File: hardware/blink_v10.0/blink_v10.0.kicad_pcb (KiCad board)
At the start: 2 copper layers, 119 x 92 mm, 130 parts, among them J1 Conn_01x02, J11 KH-BNC50-3511, J12 KH-BNC50-3511, J13 KH-BNC50-3511, J14 Conn_02x16_Odd_Even, J15 Conn_01x01, J16 Conn_01x01, J2 PJ-320D, J3 PJ-320D, J4 KH-BNC50-3511, J5 Conn_01x06_Pin, J6 Conn_01x03, J7 Conn_01x06_Pin, J9 USB_C_Receptacle, Q1 S8550, Q2 S8050, Q3 2N7002, Q4 2N7002, Q5 2N7002, SW1 SW_SPDT, SW3 LC1258OASP, SW4 SW_Push_4PDT, SW5 LC1258OASP, U1 AMS1117-3.3, U10 TMP102xxDRL, U2 AD8397, U3 M24C02-RMN, U4 STM32F405RGTx, U5 SN74LVC1G14DBV, U6 SN74LVC1G14DBV, U7 CH340C, U8 USBLC6-2P6, U9 MCP73832-2-OT, X1 GTXO-14V (2.048MHz), Y1 16MHz

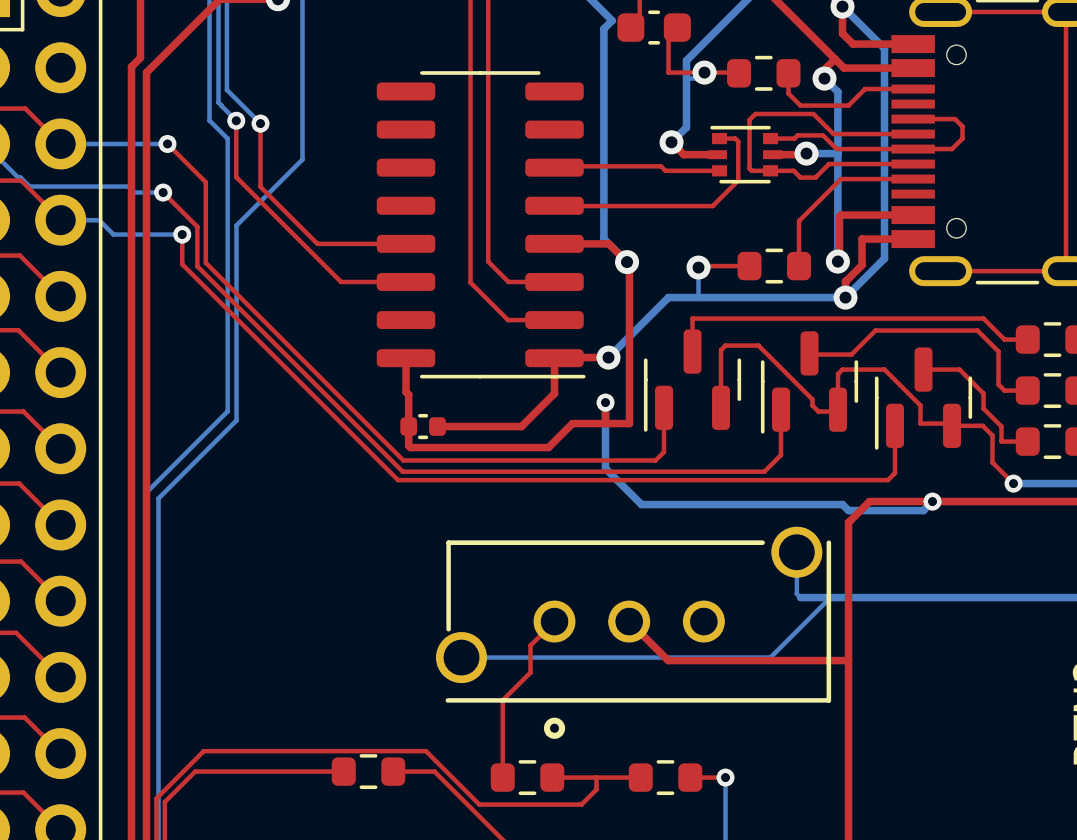
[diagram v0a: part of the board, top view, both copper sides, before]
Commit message: Fixes #211 led setting when not running
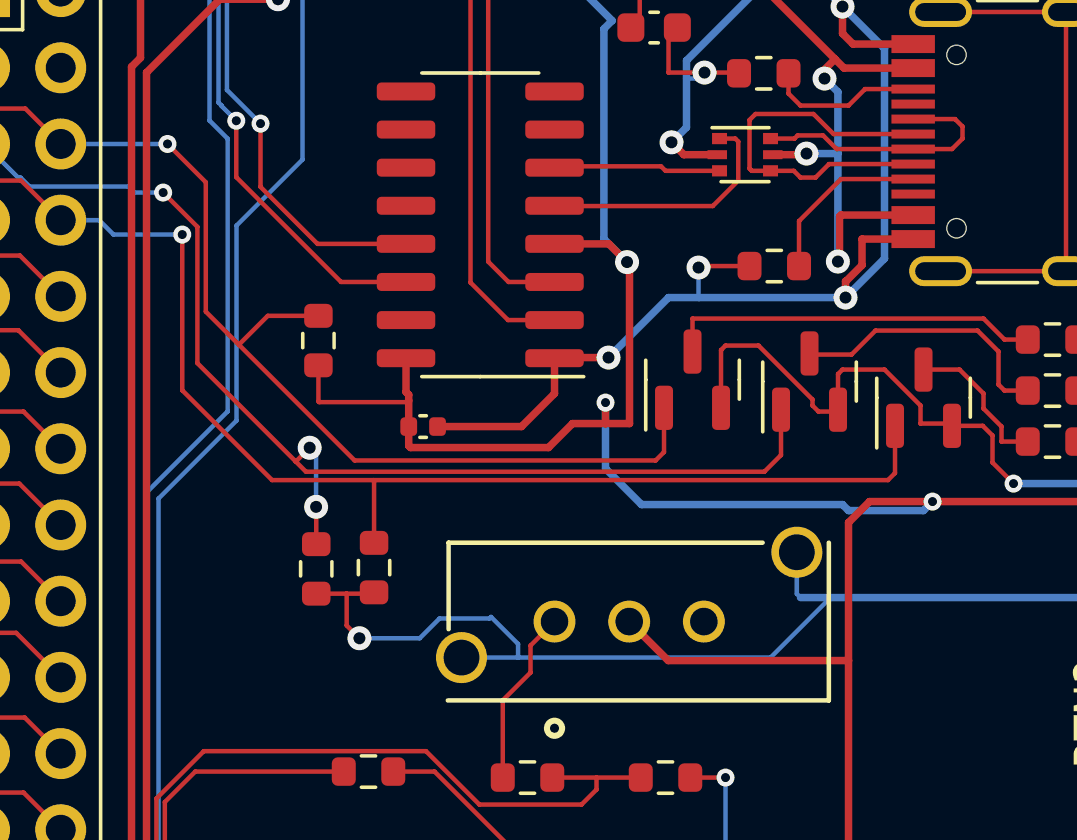
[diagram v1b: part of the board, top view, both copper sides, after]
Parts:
- added R51: 47K, Resistor_SMD:R_0603_1608Metric, F.Cu at (202.1, 72.6)
- added R52: 47K, Resistor_SMD:R_0603_1608Metric, F.Cu at (202.1, 80.2)
- added R53: 47K, Resistor_SMD:R_0603_1608Metric, F.Cu at (204.0, 80.2)
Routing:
- net GND: track 1119.8 -> 1129.8 mm, vias 46 -> 47
- net /LEDMG: track 73.8 -> 79.6 mm, vias 1 -> 3
- net /LEDMY: track 87.0 -> 91.5 mm
- net +3.3V: track 528.6 -> 532.9 mm
- net /LEDMR: track 71.7 -> 75.7 mm

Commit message: change LEDMY to LEDMB. Fixes #230
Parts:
- R21, R22: value 5k1 -> 5K1
- U10: value TMP102xxDRL -> TMP112AIDRLR
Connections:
- net /LEDMY renamed /LEDMB
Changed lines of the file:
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@@
   (net 14 "/Mic")
   (net 15 "/BOOT1")
-  (net 16 "/LEDMY")
+  (net 16 "/LEDMB")
   (net 17 "/NCOL3")
   (net 18 "/NCOL2")
@@
       (stroke (width 0.1) (type solid)) (layer "F.Fab"))
     (pad "1" smd roundrect (at -0.9375 -0.95 90) (size 1.475 0.6) (layers "F.Cu" "F.Paste" "F.Mask") (roundrect_rratio 0.25)
-      (net 16 "/LEDMY") (pinfunction "G") (pintype "input"))
+      (net 16 "/LEDMB") (pinfunction "G") (pintype "input"))
     (pad "2" smd roundrect (at -0.9375 0.95 90) (size 1.475 0.6) (layers "F.Cu" "F.Paste" "F.Mask") (roundrect_rratio 0.25)
       (net 21 "GND") (pinfunction "S") (pintype "passive"))
@@
       (net 11 "/NCOL1") (pinfunction "Pin_7") (pintype "passive"))
     (pad "8" thru_hole oval locked (at 2.54 7.62) (size 1.7 1.7) (drill 1) (layers "*.Cu" "*.Mask")
-      (net 16 "/LEDMY") (pinfunction "Pin_8") (pintype "passive"))
+      (net 16 "/LEDMB") (pinfunction "Pin_8") (pintype "passive"))
     (pad "9" thru_hole oval locked (at 0 10.16) (size 1.7 1.7) (drill 1) (layers "*.Cu" "*.Mask")
       (net 17 "/NCOL3") (pinfunction "Pin_9") (pintype "passive"))
@@
     (descr "SOT563")
     (tags "SOT-563")
-    (property "JLCPCB Part #" "C99269")
+    (property "JLCPCB Part #" "C28927")
+    (property "JLCPCB Rotation Offset" "180")
     (property "Sheetfile" "blink_v10.0.kicad_sch")
     (property "Sheetname" "")
@@
         (effects (font (size 1 1) (thickness 0.15)))
     )
-    (fp_text value "TMP102xxDRL" (at 0 1.75) (layer "F.Fab")
+    (fp_text value "TMP112AIDRLR" (at 0 1.75) (layer "F.Fab")
         (effects (font (size 1 1) (thickness 0.15)))
     )
@@
         (effects (font (size 1 1) (thickness 0.15)))
     )
-    (fp_text value "5k1" (at 0 1.43) (layer "F.Fab")
+    (fp_text value "5K1" (at 0 1.43) (layer "F.Fab")
         (effects (font (size 1 1) (thickness 0.15)))
     )
@@
         (effects (font (size 1 1) (thickness 0.15)))
     )
-    (fp_text value "5k1" (at 0 1.43) (layer "F.Fab")
+    (fp_text value "5K1" (at 0 1.43) (layer "F.Fab")
         (effects (font (size 1 1) (thickness 0.15)))
     )
@@
       (net 11 "/NCOL1") (pinfunction "PB6") (pintype "bidirectional"))
     (pad "59" smd roundrect (at -1.25 -5.675 90) (size 0.3 1.55) (layers "F.Cu" "F.Paste" "F.Mask") (roundrect_rratio 0.25)
-      (net 16 "/LEDMY") (pinfunction "PB7") (pintype "bidirectional"))
+      (net 16 "/LEDMB") (pinfunction "PB7") (pintype "bidirectional"))
     (pad "60" smd roundrect (at -1.75 -5.675 90) (size 0.3 1.55) (layers "F.Cu" "F.Paste" "F.Mask") (roundrect_rratio 0.25)
       (net 45 "/BOOT0") (pinfunction "BOOT0") (pintype "input"))
@@
       (net 21 "GND") (pintype "passive"))
     (pad "2" smd roundrect (at 0.825 0 90) (size 0.8 0.95) (layers "F.Cu" "F.Paste" "F.Mask") (roundrect_rratio 0.25)
-      (net 16 "/LEDMY") (pintype "passive"))
+      (net 16 "/LEDMB") (pintype "passive"))
     (model "${KICAD6_3DMODEL_DIR}/Resistor_SMD.3dshapes/R_0603_1608Metric.wrl"
       (offset (xyz 0 0 0))

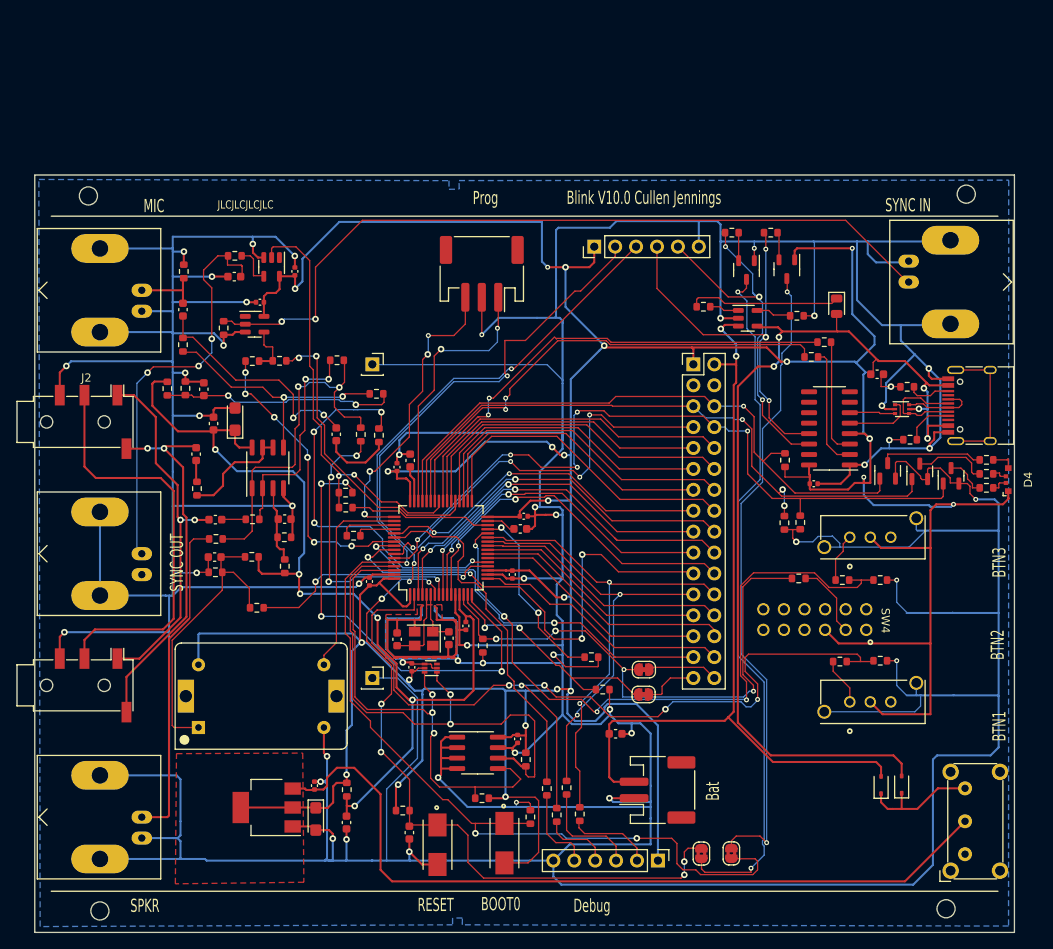
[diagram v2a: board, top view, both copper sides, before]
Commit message: clean up LED5/6 problem and BTN2
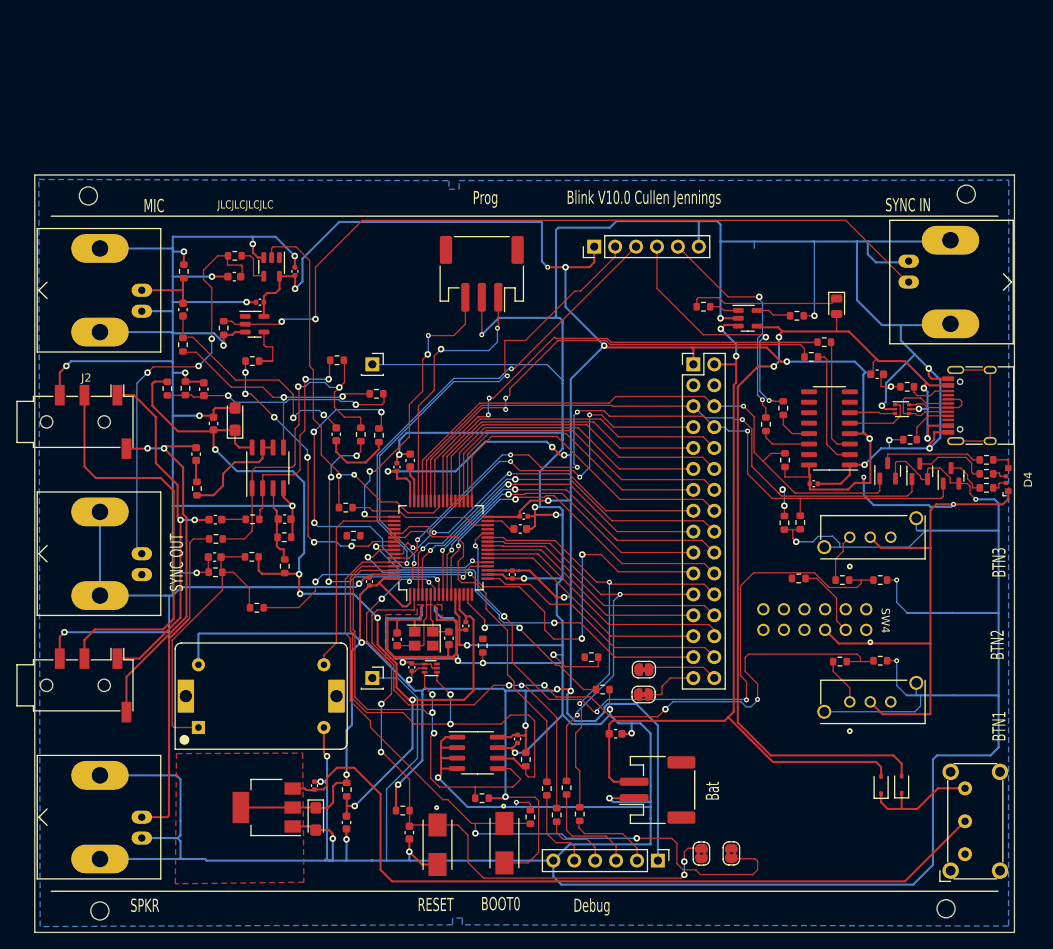
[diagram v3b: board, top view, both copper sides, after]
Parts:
- removed Q1: S8550, Package_TO_SOT_SMD:SOT-23-3
- removed Q2: S8050, Package_TO_SOT_SMD:SOT-23-3
- removed R37, R38: 1K0, Resistor_SMD:R_0603_1608Metric
- moved R29 59.6 mm to (199.8, 68.3), turned to -90 degrees
- moved R20 54.1 mm to (201.9, 66.3), turned to 90 degrees
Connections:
- JP1 pad 1: /AUX_GPS_PPS -> /GPS_TX1
- JP2 pad 1: /AUX_CLK -> /GPS_RX1
- JP3 pad 2: Net-(JP3-B) -> unconnected-(JP3-B-Pad2)
- JP4 pad 2: Net-(JP4-B) -> unconnected-(JP4-B-Pad2)
- R20 pad 1: PPS_OUT -> Net-(U7-~{DTR})
- R20 pad 2: /AUX_MON_PPS -> /USB_DTR
- R26 pad 1: /GPS_TX1 -> /AUX_MON_PPS
- R26 pad 2: /GPS_RX1 -> GND
- R29 pad 1: AUX_SYNC_IN -> /USB_RTS
- R29 pad 2: Net-(R28-Pad2) -> Net-(U7-~{RTS})
- R31 pad 1: /GPS_PPS -> /AUX_CLK
- R33 pad 1: /AUX_CLK -> /AUX_SYNC_IN
- R35 pad 2: /AUX_CLK -> /GPS_PPS
- U4 pad 37: AUX_SYNC_IN -> /AUX_SYNC_IN
- U7 pad 13: /USB_DTR -> Net-(U7-~{DTR})
- U7 pad 14: /USB_RTS -> Net-(U7-~{RTS})
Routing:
- net Net-(JP3-B): track 84.6 -> 0.00 mm, vias 2 -> 0
- net Net-(JP4-B): track 78.2 -> 0.00 mm, vias 2 -> 0
- net /AUX_CLK: track 66.8 -> 0.00 mm, vias 4 -> 0
- net /AUX_MON_PPS: track 56.3 -> 0.00 mm, vias 4 -> 0
- net AUX_SYNC_IN: track 36.4 -> 0.00 mm, vias 2 -> 0
- net +3.3V: track 532.9 -> 508.7 mm, vias 22 -> 21
- net /GPS_PPS: track 22.9 -> 0.00 mm, vias 2 -> 0
- net /USB_DTR: track 49.6 -> 31.1 mm, vias 3 -> 2
- net /USB_RTS: track 45.0 -> 28.3 mm, vias 3 -> 2
- net /AUX_GPS_PPS: track 30.7 -> 21.8 mm
- net /GPS_RX1: track 6.84 -> 0.00 mm
- net Net-(U7-~{RTS}): track 0.00 -> 6.35 mm
- net /GPS_TX1: track 4.83 -> 0.00 mm
- net Net-(U7-~{DTR}): track 0.00 -> 4.76 mm
- net Net-(Q2-B): track 3.40 -> 0.00 mm
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
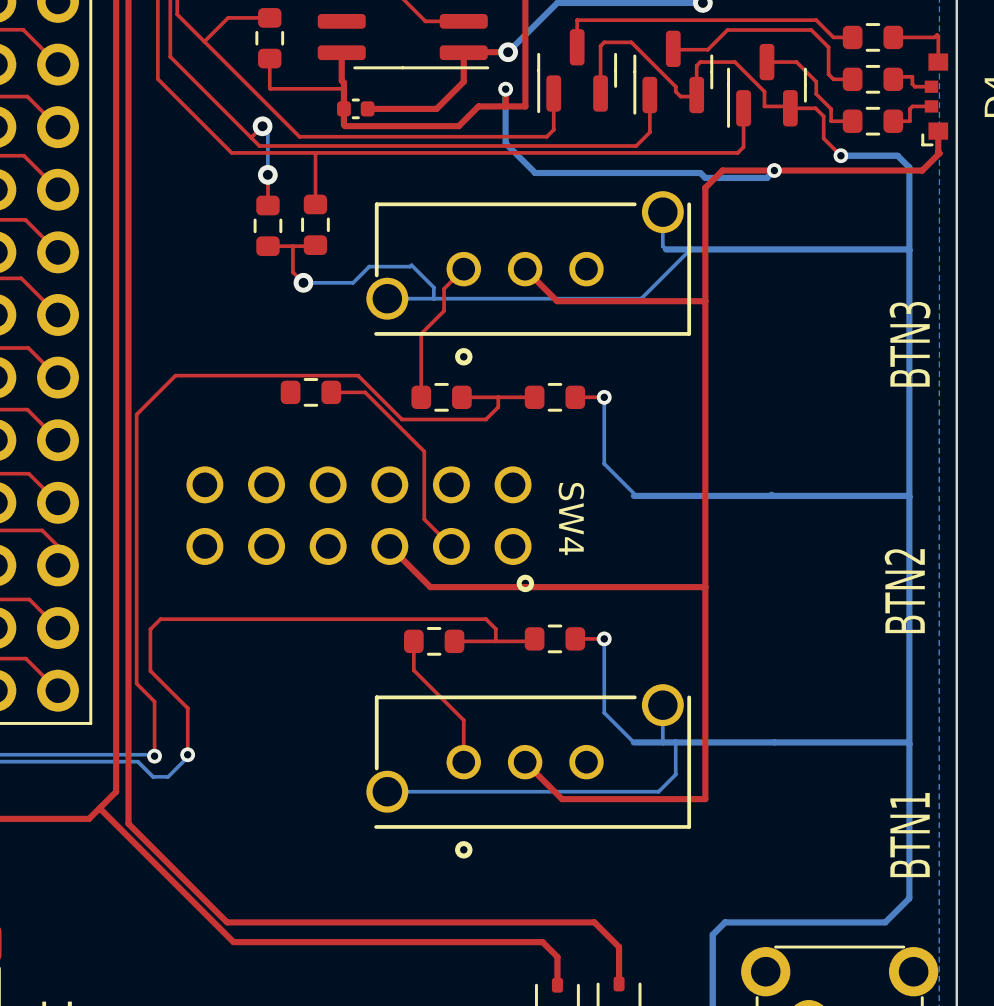
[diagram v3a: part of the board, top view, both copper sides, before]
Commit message: fix buttons. Fixes #264 Fixes #261
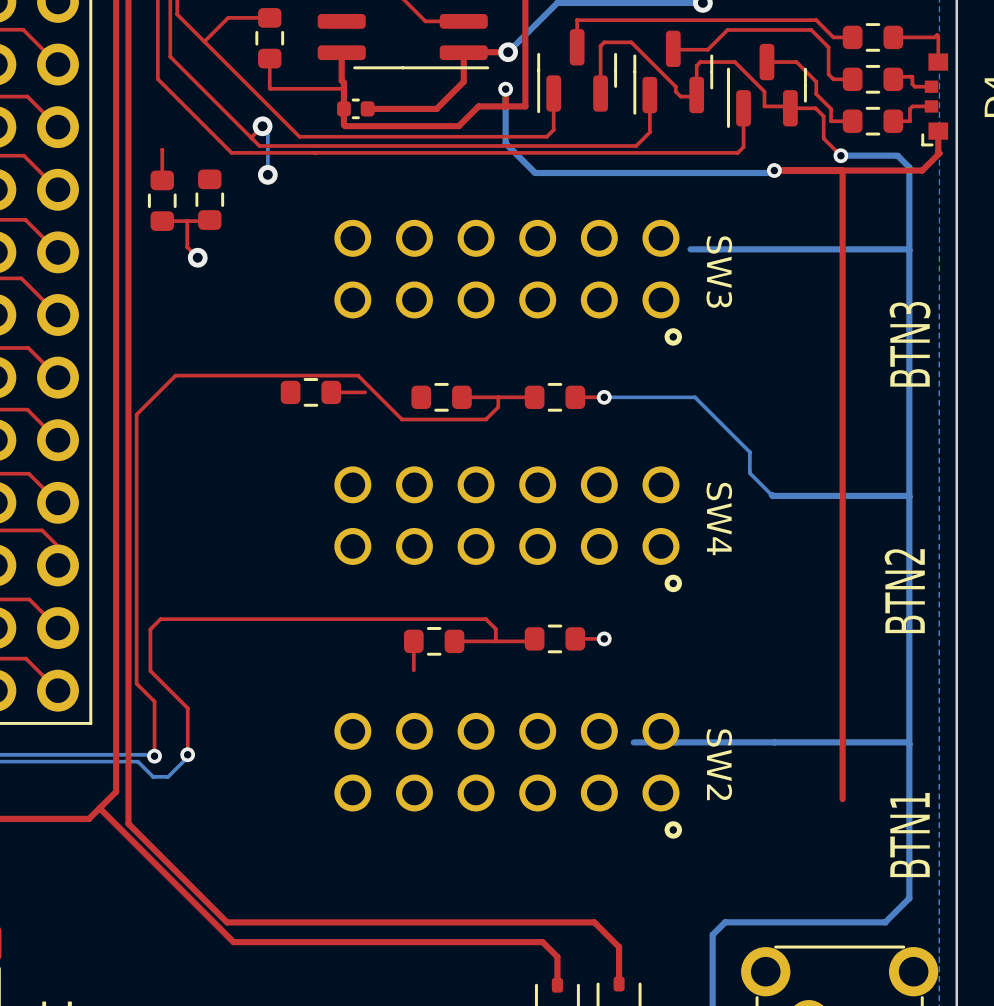
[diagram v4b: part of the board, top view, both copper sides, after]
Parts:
- removed SW5: LC1258OASP, blinky_footprints:LC1258OASP
- added SW2: SW_Push_4PDT, blinky_footprints:PBH4UOANAGX, F.Cu at (218.0, 103.2)
- SW3: value LC1258OASP -> SW_Push_4PDT; footprint blinky_footprints:LC1258OASP -> blinky_footprints:PBH4UOANAGX
- moved SW3 20.4 mm to (218.0, 83.2), turned to -90 degrees
- moved SW4 6.00 mm to (218.0, 93.2)
- moved R52 4.41 mm to (197.8, 79.2)
- moved R53 4.41 mm to (199.7, 79.2)
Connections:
- SW3 pad 1: Net-(R36-Pad1) -> unconnected-(SW3-A-Pad1)
- SW3 pad 2: +3.3V -> Net-(R25-Pad1)
- SW3 pad 3: unconnected-(SW3-Pad3) -> +3.3V
- SW3 pad 4: GND -> unconnected-(SW3-A-Pad4)
- SW3 pad 5: GND -> unconnected-(SW3-B-Pad5)
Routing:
- net GND: track 1128.3 -> 1085.5 mm
- net +3.3V: track 508.7 -> 479.6 mm
- net Net-(R35-Pad1): track 9.07 -> 1.38 mm
- net Net-(R25-Pad1): track 5.91 -> 0.00 mm
- net Net-(R36-Pad1): track 5.74 -> 1.18 mm
- net /LEDMB: track 91.5 -> 89.5 mm
